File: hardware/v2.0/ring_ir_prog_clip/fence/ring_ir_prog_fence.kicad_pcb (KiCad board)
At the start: 2 copper layers, 22.5 x 24 mm, 0 parts

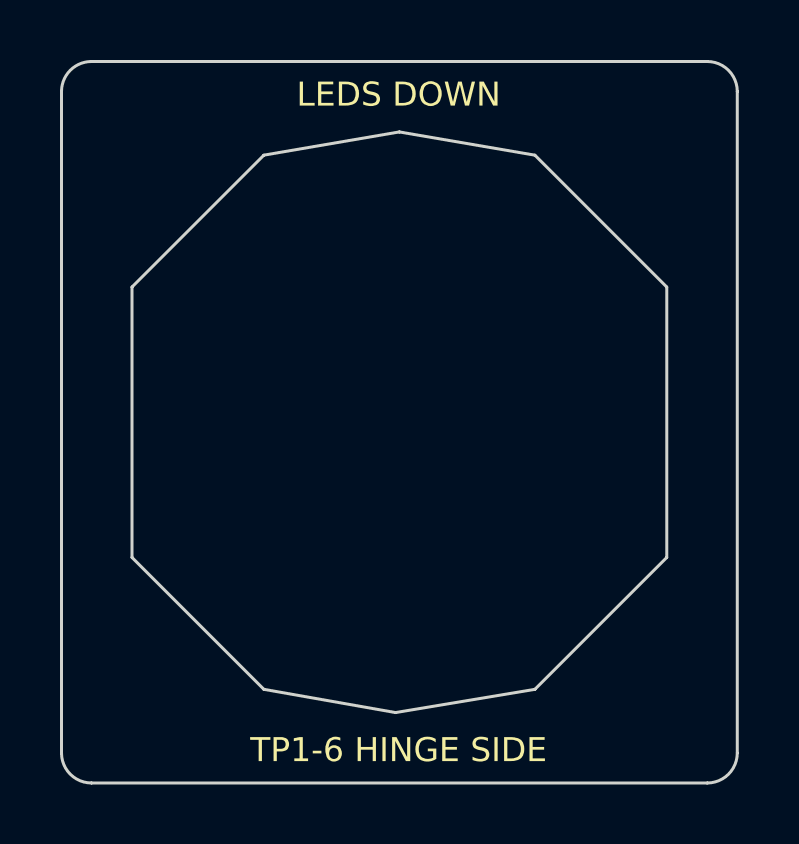
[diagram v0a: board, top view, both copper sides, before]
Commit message: IR prog clip: estimated clip dimensions and FreeCAD virtual fit check
Co-authored-by: Copilot <223556219+Copilot@users.noreply.github.com>
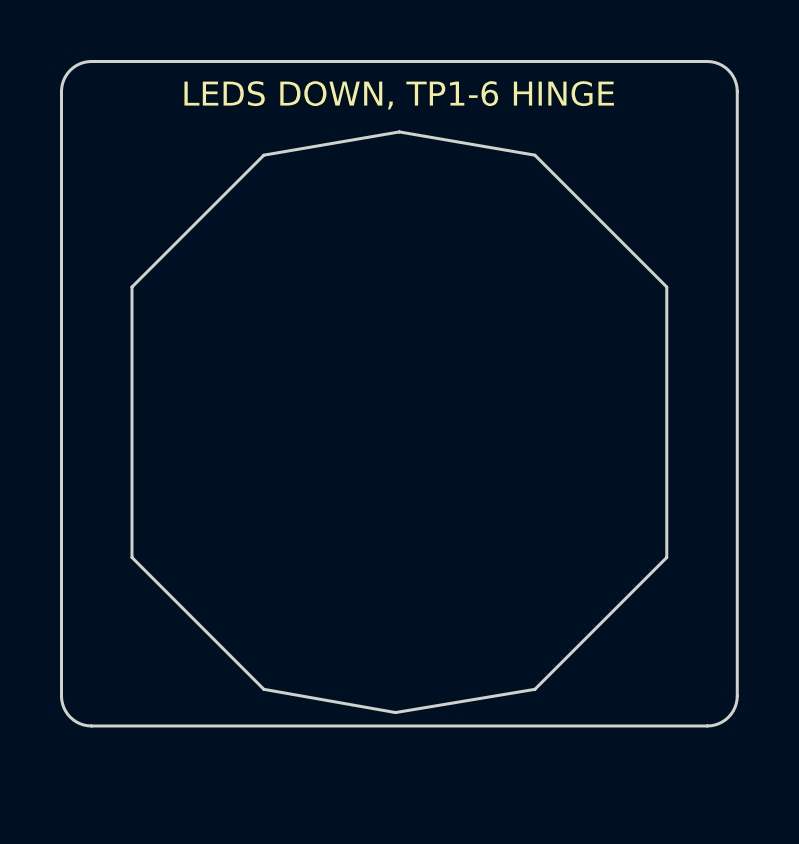
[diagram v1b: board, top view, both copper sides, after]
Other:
- board size 22.5 x 24 mm -> 22.5 x 22.2 mm
- board text added: "LEDS DOWN, TP1-6 HINGE"
- board text removed: "LEDS DOWN"
- board text removed: "TP1-6 HINGE SIDE"
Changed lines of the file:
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@@
 	)
 	(gr_line
-		(start 138.7624 106.3514)
+		(start 138.7624 104.4514)
 		(end 138.7624 84.3014)
 		(stroke
@@
 	)
 	(gr_arc
-		(start 139.7624 107.3514)
-		(mid 139.055293 107.058506)
-		(end 138.7624 106.3514)
+		(start 139.7624 105.4514)
+		(mid 139.055293 105.158506)
+		(end 138.7624 104.4514)
 		(stroke
 			(width 0.1)
@@
 	)
 	(gr_line
-		(start 160.2884 107.3514)
-		(end 139.7624 107.3514)
+		(start 160.2884 105.4514)
+		(end 139.7624 105.4514)
 		(stroke
 			(width 0.1)
@@
 	(gr_line
 		(start 161.2884 84.3014)
-		(end 161.2884 106.3514)
+		(end 161.2884 104.4514)
 		(stroke
 			(width 0.1)
@@
 	)
 	(gr_arc
-		(start 161.2884 106.3514)
-		(mid 160.995506 107.058506)
-		(end 160.2884 107.3514)
+		(start 161.2884 104.4514)
+		(mid 160.995506 105.158506)
+		(end 160.2884 105.4514)
 		(stroke
 			(width 0.1)
@@
 		(layer "Edge.Cuts")
 	)
-	(gr_text "LEDS DOWN"
+	(gr_text "LEDS DOWN, TP1-6 HINGE"
 		(at 150 84.4014 0)
 		(layer "F.SilkS")
 		(effects
-			(font
-				(size 0.8 0.8)
-				(thickness 0.12)
-			)
-		)
-	)
-	(gr_text "TP1-6 HINGE SIDE"
-		(at 150 106.2514 0)
-		(layer "F.SilkS")
-		(effects
